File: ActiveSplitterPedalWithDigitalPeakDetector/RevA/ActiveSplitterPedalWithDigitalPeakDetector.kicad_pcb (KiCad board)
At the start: 2 copper layers, 112.5 x 86.4 mm, 101 parts, among them J1 MonoJack2Switch, J2 Barrel_Jack, J3 MonoJack2Switch, J4 MonoJack2Switch, J5 MonoJack2Switch, J6 MonoJack2Switch, J7 Conn_01x05, U1 MCP1703A-3302_SOT223, U10 MCP601-xOT, U11 TL072, U13 TPS60400, U14 TPS60400, U15 TPS60400, U16 MCP601-xOT, U17 MCP601-xOT, U2 TL072, U3 TPS60400, U4 STM32F051K8Tx, U5 TL072, U7 MCP601-xOT, U8 TL072

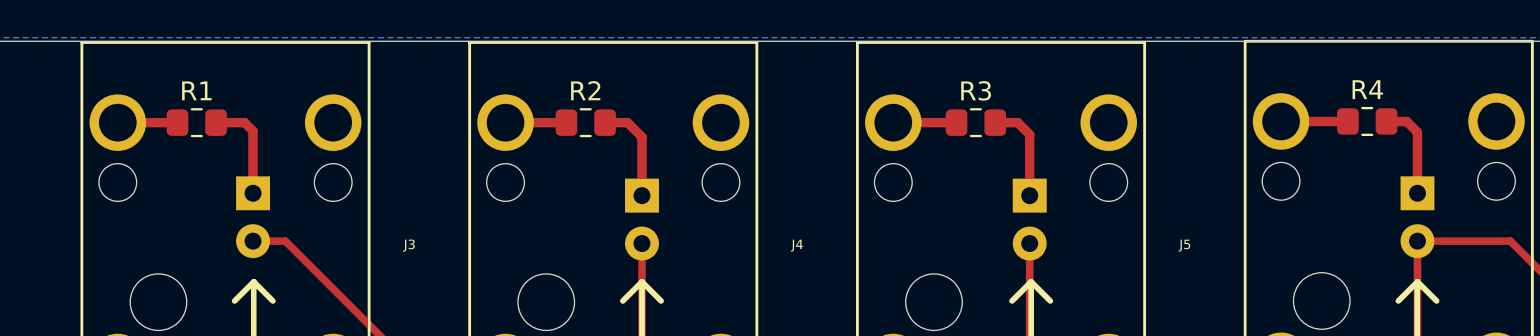
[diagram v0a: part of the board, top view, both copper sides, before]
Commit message: hw update
moved led resistors to back copper layer
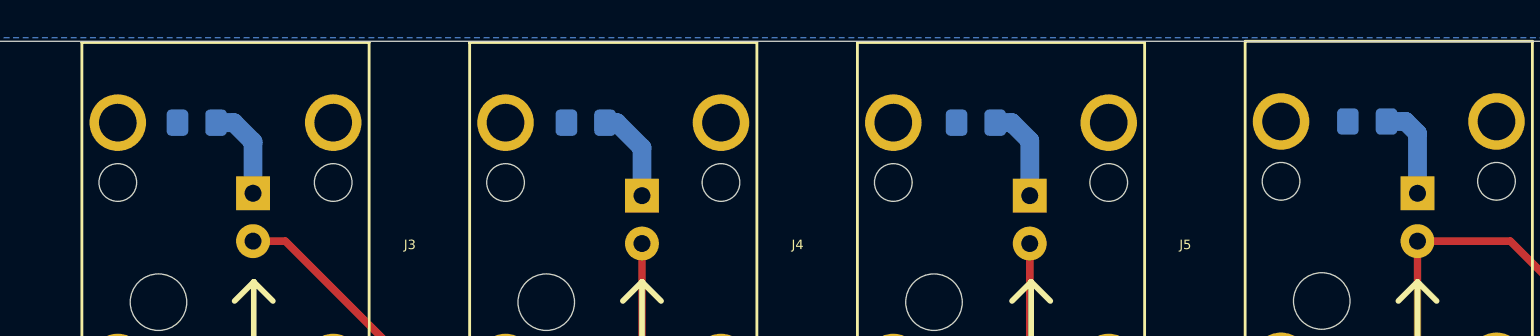
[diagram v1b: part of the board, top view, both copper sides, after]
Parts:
- R1, R2, R3, R4: moved to B.Cu
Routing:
- net GNDS: track 100.6 -> 87.3 mm

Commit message: schematic update
updated resistor (Rin) to 1K/10K
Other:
- board text removed: "+3V"
- board text removed: "-3V"
